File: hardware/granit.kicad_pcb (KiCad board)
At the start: 4 copper layers, 92 x 100 mm, 112 parts, among them IC1 ASM1061, J1 12V Barrel, J2 12V Screw Terminal, J3 RJ45_RB1-125B8G1A, J6 Conn_01x02, J7 USB_C_Receptacle_USB2.0_14P, J8 Conn_01x03, J9 SATA_22pin, Q1 FDS4435BZ, Q2 FDS4435BZ, Q3 FDS4435BZ, Q4 2N7002, Q5 2N7002, Q6 2N7002, SW1 SW_Push, U1 NCP1117-3.3_SOT223, U2 AP64501SP-13, U3 74AHCT1G125, U4 DS3231MZ, U5 USBLC6-2SC6, U6 74AHCT1G32, Y1 Crystal

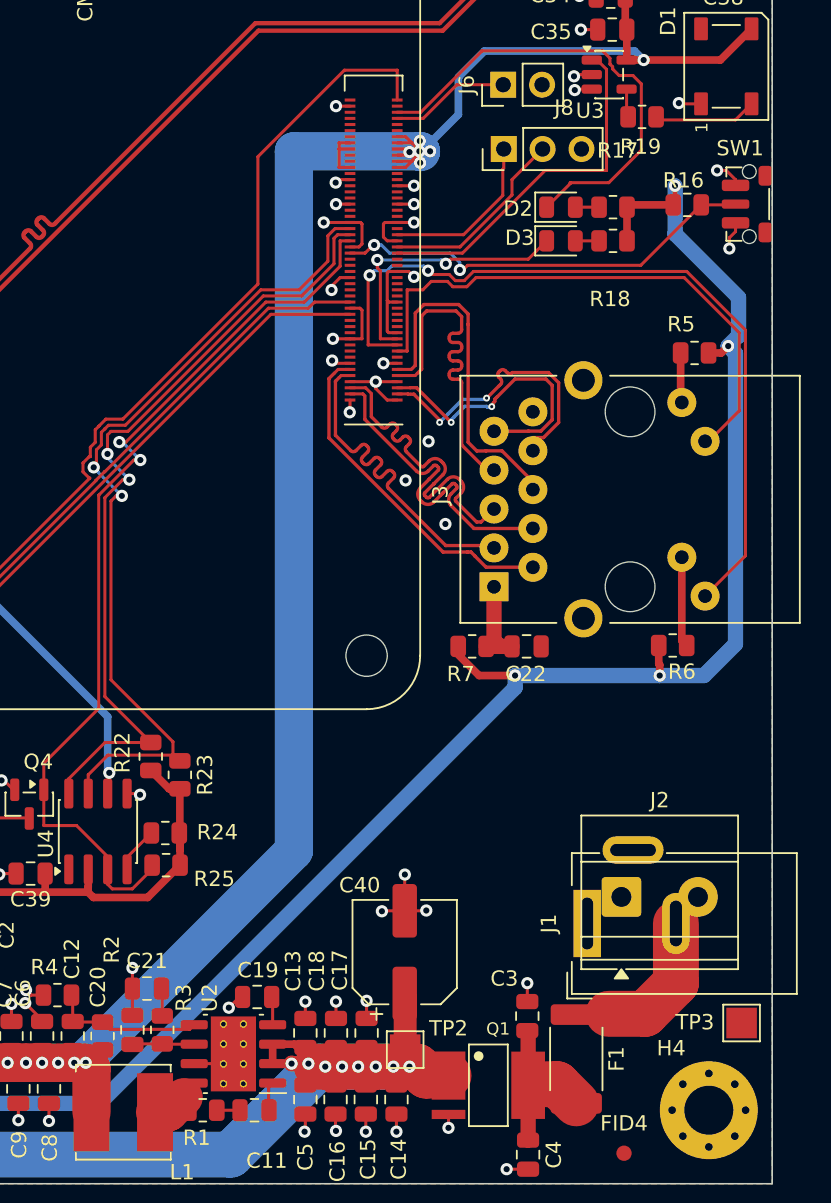
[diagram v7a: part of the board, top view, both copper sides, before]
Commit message: Move J1/J2 to separate locations, resolve silk overlap violations
- Separate barrel jack (J1) and screw terminal (J2) placement
- Eliminates silk overlap and silk_over_copper warnings between J1/J2
- DRC violations reduced from 30 to 23
- Remaining: silk cosmetic (15), starved thermals (6), hole-to-hole (1),
  lib footprint mismatch (1)
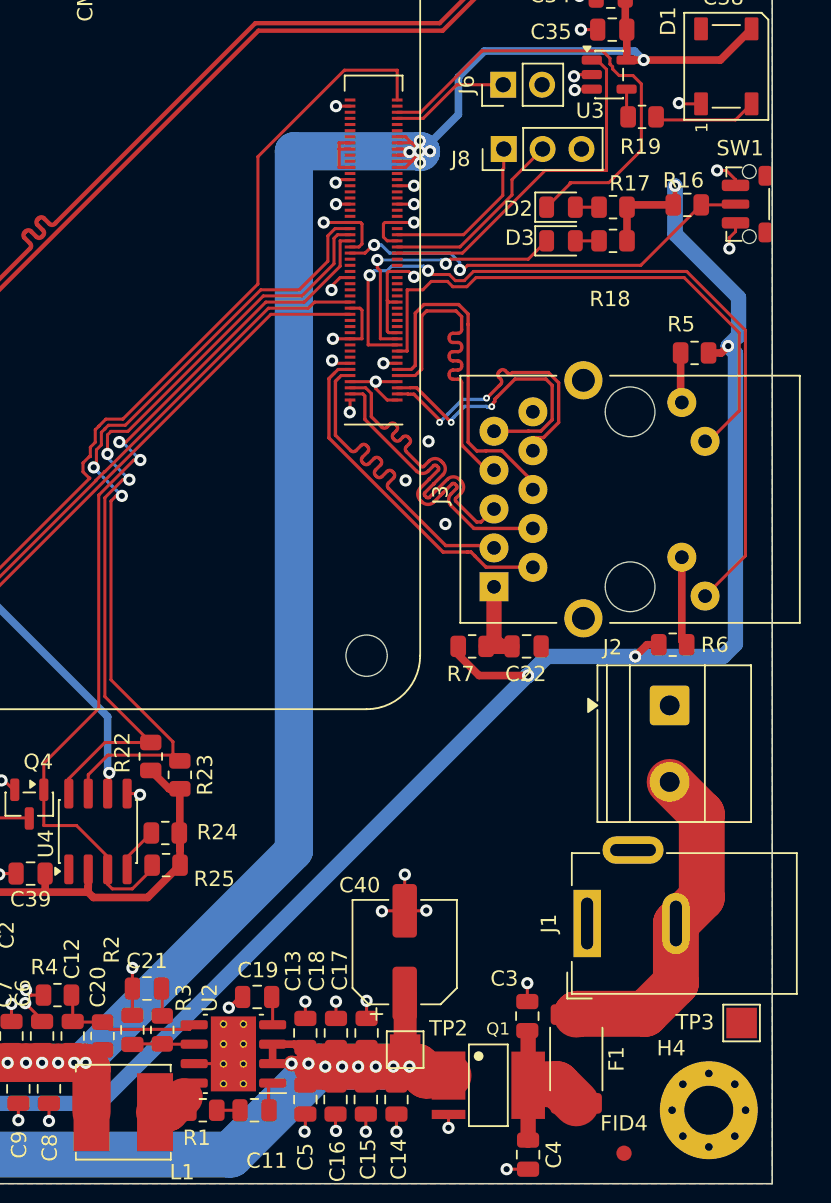
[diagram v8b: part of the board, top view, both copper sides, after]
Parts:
- moved J2 12.9 mm to (105.3, 88.8), turned to -90 degrees
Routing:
- net /Power Supply/unfused: track 9.13 -> 22.1 mm
